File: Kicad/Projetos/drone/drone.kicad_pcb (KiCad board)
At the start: 2 copper layers, 20 parts, among them M1 Motor_Servo, M10 Motor_Servo, M11 Motor_Servo, M12 Motor_Servo, M13 Motor_Servo, M14 Motor_Servo, M15 Motor_Servo, M16 Motor_Servo, M17 Motor_Servo, M18 Motor_Servo, M2 Motor_Servo, M3 Motor_Servo, M4 Motor_Servo, M5 Motor_Servo, M6 Motor_Servo, M7 Motor_Servo, M8 Motor_Servo, M9 Motor_Servo, U1 SC0195_9_, U3 DEVKIT_V1_ESP32-WROOM-32

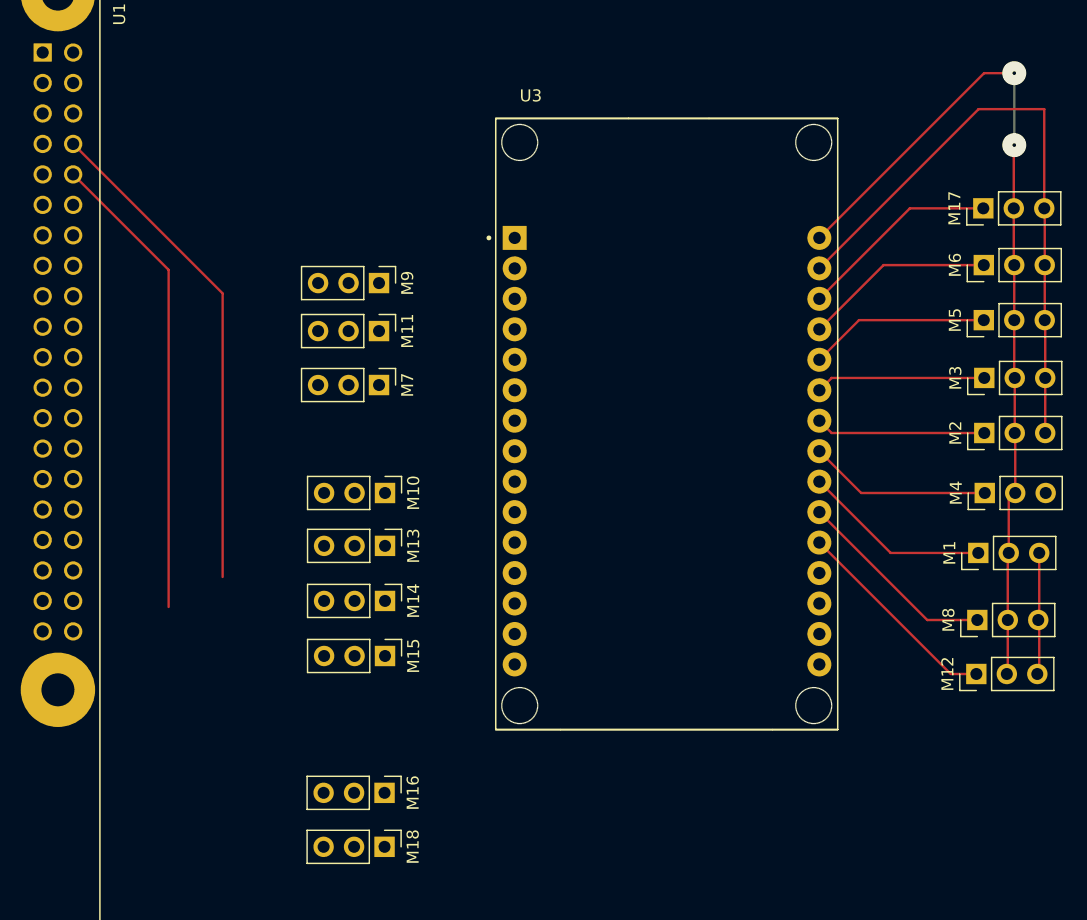
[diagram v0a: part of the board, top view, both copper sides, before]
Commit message: roteamento, servos - esp32
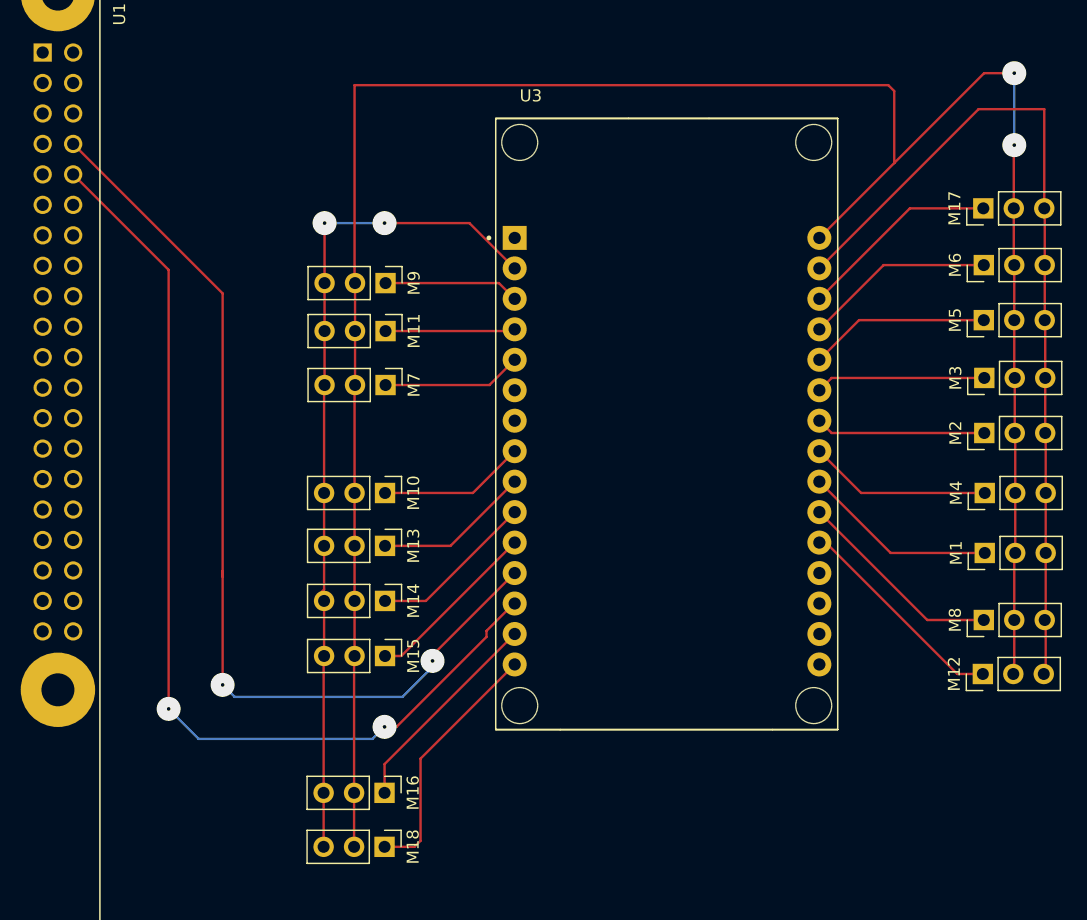
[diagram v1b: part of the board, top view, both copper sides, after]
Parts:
- moved M11 0.54 mm to (150.6, 80.0)
- moved M7 0.54 mm to (150.6, 84.5)
- moved M8 0.54 mm to (200.5, 104.1)
- moved M9 0.54 mm to (150.6, 76.0)
- moved M1 0.54 mm to (200.5, 98.5)
- moved M12 0.54 mm to (200.4, 108.6)
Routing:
- net +5V: track 73.2 -> 188.2 mm
- net GND: track 61.4 -> 141.8 mm, vias 0 -> 2
- net tx: track 39.4 -> 82.7 mm, vias 0 -> 2
- net rx: track 41.3 -> 80.4 mm, vias 0 -> 2
- net /Raiz/perna 6 coxa: track 0.00 -> 21.2 mm
- net /Raiz/perna 6 femur: track 0.00 -> 17.7 mm
- net /Raiz/perna 5 coxa: track 0.00 -> 14.7 mm
- net /Raiz/perna 5 femur: track 0.00 -> 13.9 mm
- net /Raiz/perna 5 tibia: track 0.00 -> 13.0 mm
- net /Raiz/perna 4 coxa: track 0.00 -> 12.3 mm
- net /Raiz/perna 3 coxa: track 0.00 -> 11.6 mm
- net /Raiz/perna 3 tibia: track 0.00 -> 11.3 mm
- net /Raiz/perna 4 femur: track 0.00 -> 10.8 mm
- net /Raiz/perna 3 femur: track 16.9 -> 17.4 mm
- net /Raiz/perna 1 coxa: track 15.7 -> 16.3 mm

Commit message: capacitores de desacoplamento no kicad
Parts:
- added C10: 100nF, Capacitor_THT:C_Disc_D7.0mm_W2.5mm_P5.00mm, F.Cu at (257.9, 58.2)
- added C11: 100nF, Capacitor_THT:C_Disc_D7.0mm_W2.5mm_P5.00mm, F.Cu at (266.5, 29.9)
- added C12: 100nF, Capacitor_THT:C_Disc_D7.0mm_W2.5mm_P5.00mm, F.Cu at (266.5, 34.0)
- added C13: 100nF, Capacitor_THT:C_Disc_D7.0mm_W2.5mm_P5.00mm, F.Cu at (266.5, 38.0)
- added C14: 100nF, Capacitor_THT:C_Disc_D7.0mm_W2.5mm_P5.00mm, F.Cu at (266.5, 42.0)
- added C15: 100nF, Capacitor_THT:C_Disc_D7.0mm_W2.5mm_P5.00mm, F.Cu at (266.5, 46.1)
- added C16: 100nF, Capacitor_THT:C_Disc_D7.0mm_W2.5mm_P5.00mm, F.Cu at (266.5, 50.1)
- added C17: 100nF, Capacitor_THT:C_Disc_D7.0mm_W2.5mm_P5.00mm, F.Cu at (266.5, 54.2)
- added C18: 100nF, Capacitor_THT:C_Disc_D7.0mm_W2.5mm_P5.00mm, F.Cu at (266.5, 58.2)
- added C19: 100nF, Capacitor_THT:C_Disc_D7.0mm_W2.5mm_P5.00mm, F.Cu at (266.5, 26.1)
- added C2: 47uF, Capacitor_THT:C_Disc_D7.0mm_W2.5mm_P5.00mm, F.Cu at (210.0, 58.0)
- added C20: 100nF, Capacitor_THT:C_Disc_D7.0mm_W2.5mm_P5.00mm, F.Cu at (258.0, 26.0)
- added C21: 100nF, Capacitor_THT:C_Disc_D7.0mm_W2.5mm_P5.00mm, F.Cu at (258.0, 30.1)
- added C22: 100nF, Capacitor_THT:C_Disc_D7.0mm_W2.5mm_P5.00mm, F.Cu at (258.0, 34.1)
- added C23: 47uF, Capacitor_THT:C_Disc_D7.0mm_W2.5mm_P5.00mm, F.Cu at (229.5, 58.0)
- added C24: 1000uF, Capacitor_THT:C_Disc_D7.0mm_W2.5mm_P5.00mm, F.Cu at (222.5, 58.0)
- added C3: 100nF, Capacitor_THT:C_Disc_D7.0mm_W2.5mm_P5.00mm, F.Cu at (258.0, 38.0)
- added C5: 1000uF, Capacitor_THT:C_Disc_D7.0mm_W2.5mm_P5.00mm, F.Cu at (216.0, 58.0)
- added C6: 100nF, Capacitor_THT:C_Disc_D7.0mm_W2.5mm_P5.00mm, F.Cu at (257.9, 42.0)
- added C7: 100nF, Capacitor_THT:C_Disc_D7.0mm_W2.5mm_P5.00mm, F.Cu at (257.9, 46.1)
- added C8: 100nF, Capacitor_THT:C_Disc_D7.0mm_W2.5mm_P5.00mm, F.Cu at (257.9, 50.1)
- added C9: 100nF, Capacitor_THT:C_Disc_D7.0mm_W2.5mm_P5.00mm, F.Cu at (257.9, 54.2)
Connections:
- net rx renamed rx_esp32
- net tx renamed tx_esp32
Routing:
- net +5V: track 188.2 -> 254.0 mm
- net GND: track 141.8 -> 193.7 mm, vias 2 -> 4
- net tx_esp32: track 82.7 -> 84.2 mm
